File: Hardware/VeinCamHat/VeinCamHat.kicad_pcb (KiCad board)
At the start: 2 copper layers, 65 x 56 mm, 23 parts, among them J1 Raspberry_Pi_2_3, Q1 NTJD4001N

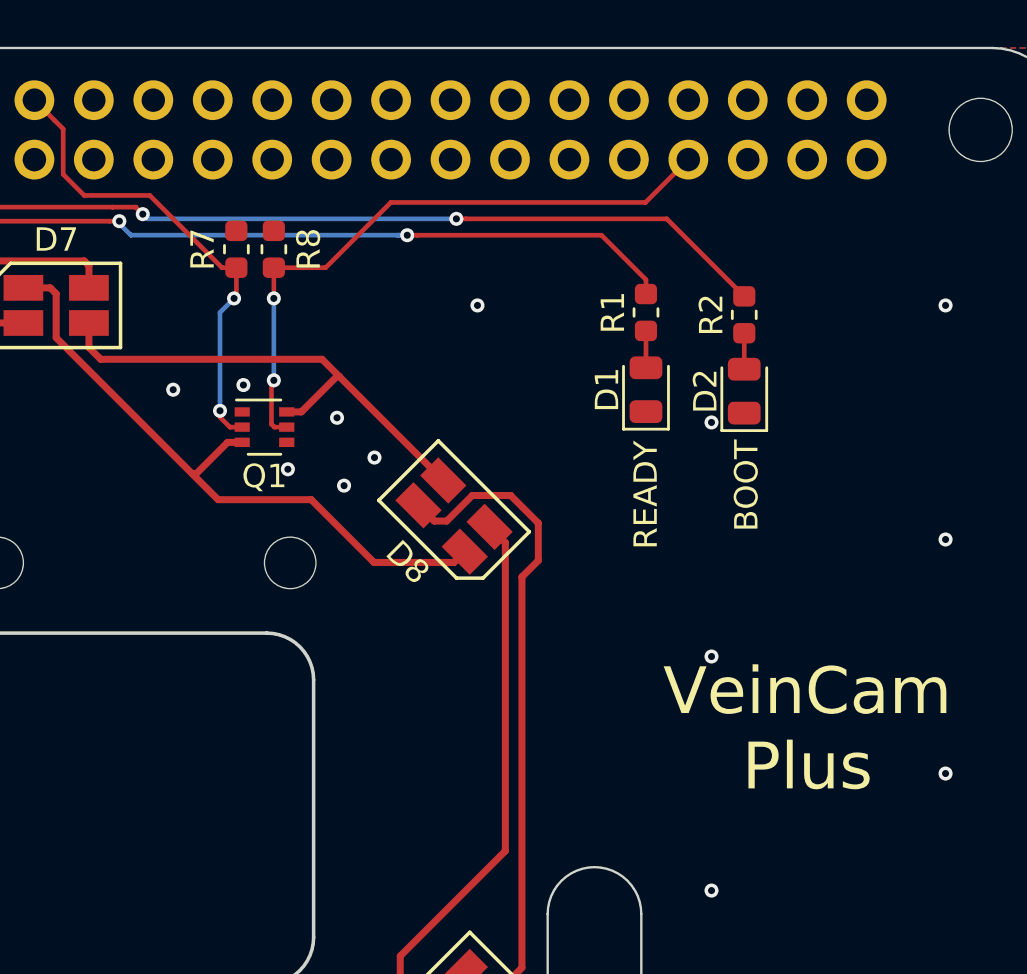
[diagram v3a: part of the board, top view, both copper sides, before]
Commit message: Finished boards, v0.2 gerbers zipped and sent off to fab
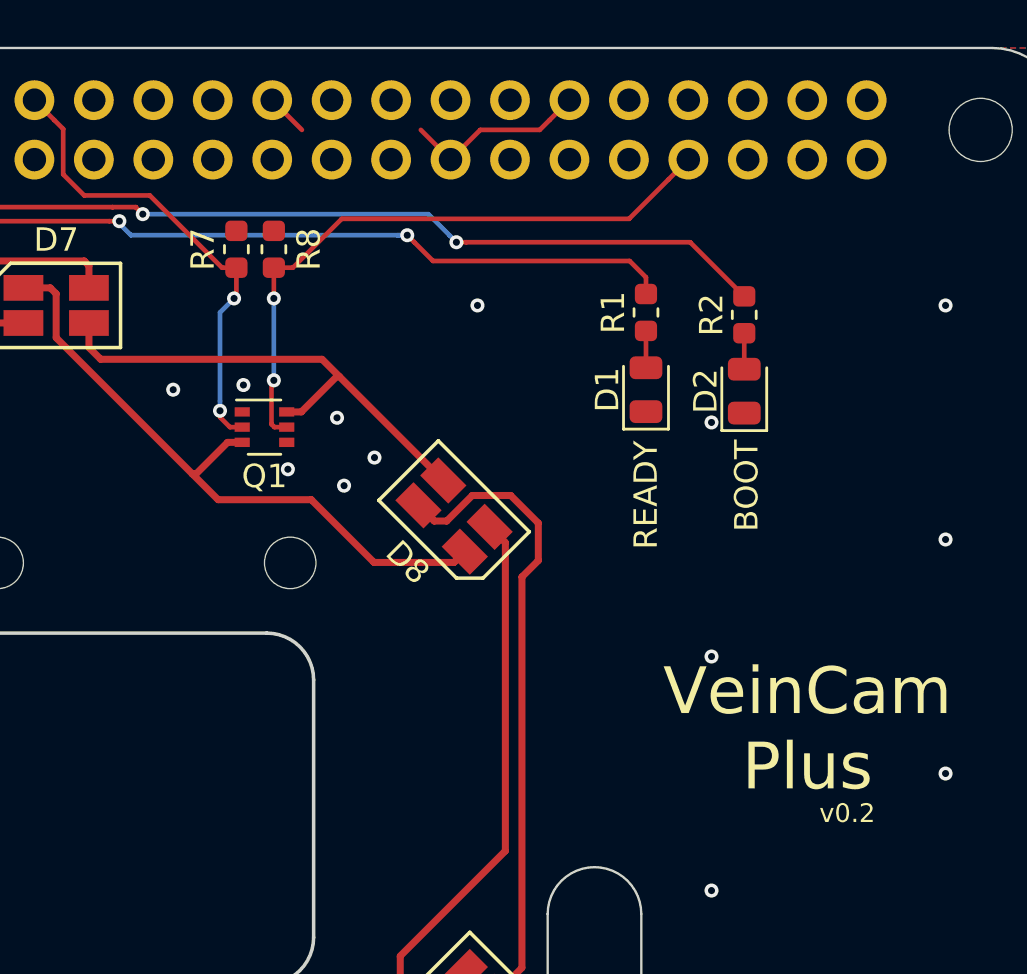
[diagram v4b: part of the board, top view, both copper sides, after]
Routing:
- net GND: track 0.00 -> 9.72 mm
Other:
- board text added: "v0.2"
- board text added: "veincam.org"
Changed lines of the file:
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@@
-(kicad_pcb (version 20171130) (host pcbnew "(5.0.2)-1")
+(kicad_pcb (version 20171130) (host pcbnew "(5.1.0)-1")
   (general
     (thickness 1.6)
-    (drawings 18)
-    (tracks 179)
+    (drawings 20)
+    (tracks 188)
     (zones 0)
     (modules 23)
@@
     (zone_45_only no)
     (trace_min 0.2)
-    (segment_width 0.1)
-    (edge_width 0.1)
     (via_size 0.6)
     (via_drill 0.3)
@@
     (uvia_min_size 0.5)
     (uvia_min_drill 0.1)
+    (edge_width 0.1)
+    (segment_width 0.1)
     (pcb_text_width 0.3)
     (pcb_text_size 1 1)
@@
     (solder_mask_min_width 0.1)
     (aux_axis_origin 200 150)
-    (visible_elements 7FFFF7FF)
+    (visible_elements 7FFFFFFF)
     (pcbplotparams
       (layerselection 0x012f8_ffffffff)
@@
     )
   )
+  (gr_text veincam.org (at 221.9 146.9) (layer B.SilkS)
+    (effects (font (size 1 1) (thickness 0.2)) (justify mirror))
+  )
+  (gr_text v0.2 (at 255.8 126.7) (layer F.SilkS)
+    (effects (font (size 0.8 0.8) (thickness 0.12)))
+  )
   (gr_text "Note: 1.6mm FR4" (at 229.8 154) (layer Cmts.User)
     (effects (font (size 1 1) (thickness 0.25)))
@@
   (via (at 207.4 148.1) (size 0.6) (drill 0.3) (layers F.Cu B.Cu) (net 2))
   (via (at 219.4 148.3) (size 0.6) (drill 0.3) (layers F.Cu B.Cu) (net 2))
+  (segment (start 232.5 97.5) (end 231.23 96.23) (width 0.2) (layer F.Cu) (net 2))
+  (segment (start 238.85 98.77) (end 237.58 97.5) (width 0.2) (layer F.Cu) (net 2))
+  (segment (start 243.080001 97.079999) (end 243.93 96.23) (width 0.2) (layer F.Cu) (net 2))
+  (segment (start 242.66 97.5) (end 243.080001 97.079999) (width 0.2) (layer F.Cu) (net 2))
+  (segment (start 238.85 98.77) (end 240.12 97.5) (width 0.2) (layer F.Cu) (net 2))
+  (segment (start 240.12 97.5) (end 242.66 97.5) (width 0.2) (layer F.Cu) (net 2))
   (segment (start 247.2 106.0875) (end 247.2 107.6625) (width 0.2) (layer F.Cu) (net 3))
   (segment (start 251.4 106.1875) (end 251.4 107.725) (width 0.2) (layer F.Cu) (net 4))
@@
   (segment (start 236.575736 102) (end 237 102) (width 0.2) (layer B.Cu) (net 11))
   (via (at 237 102) (size 0.6) (drill 0.3) (layers F.Cu B.Cu) (net 11))
-  (segment (start 247.2 103.9) (end 245.3 102) (width 0.2) (layer F.Cu) (net 11))
-  (segment (start 247.2 104.5125) (end 247.2 103.9) (width 0.2) (layer F.Cu) (net 11))
-  (segment (start 245.3 102) (end 237.424264 102) (width 0.2) (layer F.Cu) (net 11))
-  (segment (start 237.424264 102) (end 237 102) (width 0.2) (layer F.Cu) (net 11))
   (segment (start 224.275736 101.4) (end 224.7 101.4) (width 0.2) (layer F.Cu) (net 11))
   (segment (start 215.99 98.77) (end 218.62 101.4) (width 0.2) (layer F.Cu) (net 11))
@@
   (segment (start 237 102) (end 225.2 102) (width 0.2) (layer B.Cu) (net 11))
   (via (at 224.7 101.4) (size 0.6) (drill 0.3) (layers F.Cu B.Cu) (net 11))
-  (segment (start 239.524264 101.3) (end 239.1 101.3) (width 0.2) (layer F.Cu) (net 12))
-  (segment (start 248.0875 101.3) (end 239.524264 101.3) (width 0.2) (layer F.Cu) (net 12))
-  (segment (start 251.4 104.6125) (end 248.0875 101.3) (width 0.2) (layer F.Cu) (net 12))
-  (via (at 239.1 101.3) (size 0.6) (drill 0.3) (layers F.Cu B.Cu) (net 12))
+  (segment (start 237.299999 102.299999) (end 237 102) (width 0.2) (layer F.Cu) (net 11))
+  (segment (start 238.1 103.1) (end 237.299999 102.299999) (width 0.2) (layer F.Cu) (net 11))
+  (segment (start 246.5 103.1) (end 238.1 103.1) (width 0.2) (layer F.Cu) (net 11))
+  (segment (start 247.2 104.5125) (end 247.2 103.8) (width 0.2) (layer F.Cu) (net 11))
+  (segment (start 247.2 103.8) (end 246.5 103.1) (width 0.2) (layer F.Cu) (net 11))
   (via (at 225.7 101.1) (size 0.6) (drill 0.3) (layers F.Cu B.Cu) (net 12))
-  (segment (start 225.9 101.3) (end 225.7 101.1) (width 0.2) (layer B.Cu) (net 12))
-  (segment (start 239.1 101.3) (end 225.9 101.3) (width 0.2) (layer B.Cu) (net 12))
   (segment (start 218.857999 100.800001) (end 224.411997 100.800001) (width 0.2) (layer F.Cu) (net 12))
   (segment (start 217.140001 99.082003) (end 218.857999 100.800001) (width 0.2) (layer F.Cu) (net 12))
@@
   (segment (start 215.99 96.23) (end 217.140001 97.380001) (width 0.2) (layer F.Cu) (net 12))
   (segment (start 217.140001 97.380001) (end 217.140001 99.082003) (width 0.2) (layer F.Cu) (net 12))
+  (segment (start 237.899998 101.1) (end 238.800001 102.000003) (width 0.2) (layer B.Cu) (net 12))
+  (segment (start 238.800001 102.000003) (end 239.1 102.300002) (width 0.2) (layer B.Cu) (net 12))
+  (segment (start 251.4 104.6125) (end 249.087502 102.300002) (width 0.2) (layer F.Cu) (net 12))
+  (segment (start 239.524264 102.300002) (end 239.1 102.300002) (width 0.2) (layer F.Cu) (net 12))
+  (segment (start 249.087502 102.300002) (end 239.524264 102.300002) (width 0.2) (layer F.Cu) (net 12))
+  (segment (start 225.7 101.1) (end 237.899998 101.1) (width 0.2) (layer B.Cu) (net 12))
+  (via (at 239.1 102.300002) (size 0.6) (drill 0.3) (layers F.Cu B.Cu) (net 12))
   (via (at 229.6 104.7) (size 0.6) (drill 0.3) (layers F.Cu B.Cu) (net 13))
   (segment (start 229.7 104.6) (end 229.7 103.3875) (width 0.2) (layer F.Cu) (net 13))
@@
   (segment (start 231.85 110.2) (end 231.325 110.2) (width 0.2) (layer F.Cu) (net 14))
   (segment (start 231.325 110.2) (end 231.2 110.075) (width 0.2) (layer F.Cu) (net 14))
-  (segment (start 247.18 100.6) (end 249.01 98.77) (width 0.2) (layer F.Cu) (net 14))
-  (segment (start 236.3 100.6) (end 247.18 100.6) (width 0.2) (layer F.Cu) (net 14))
-  (segment (start 231.3 103.3875) (end 233.5125 103.3875) (width 0.2) (layer F.Cu) (net 14))
-  (segment (start 233.5125 103.3875) (end 236.3 100.6) (width 0.2) (layer F.Cu) (net 14))
+  (segment (start 248.160001 99.619999) (end 249.01 98.77) (width 0.2) (layer F.Cu) (net 14))
+  (segment (start 246.48 101.3) (end 248.160001 99.619999) (width 0.2) (layer F.Cu) (net 14))
+  (segment (start 234.2 101.3) (end 246.48 101.3) (width 0.2) (layer F.Cu) (net 14))
+  (segment (start 231.3 103.3875) (end 232.1125 103.3875) (width 0.2) (layer F.Cu) (net 14))
+  (segment (start 232.1125 103.3875) (end 234.2 101.3) (width 0.2) (layer F.Cu) (net 14))
   (segment (start 202.5 135.520101) (end 203.47972 134.540381) (width 0.3) (layer F.Cu) (net 15))
   (segment (start 210.4125 145.2) (end 202.5 137.2875) (width 0.3) (layer F.Cu) (net 15))

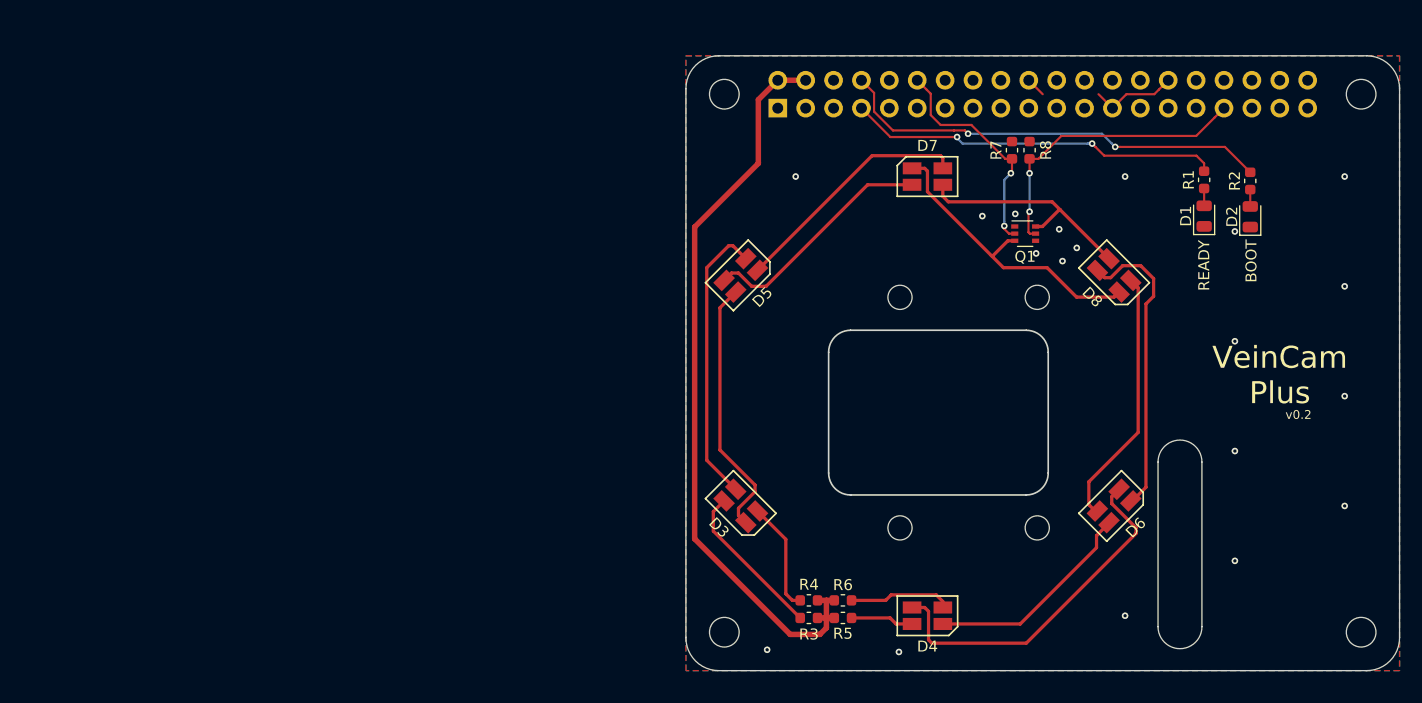
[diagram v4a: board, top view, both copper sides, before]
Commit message: changed logo direction on veincam, added licencing document
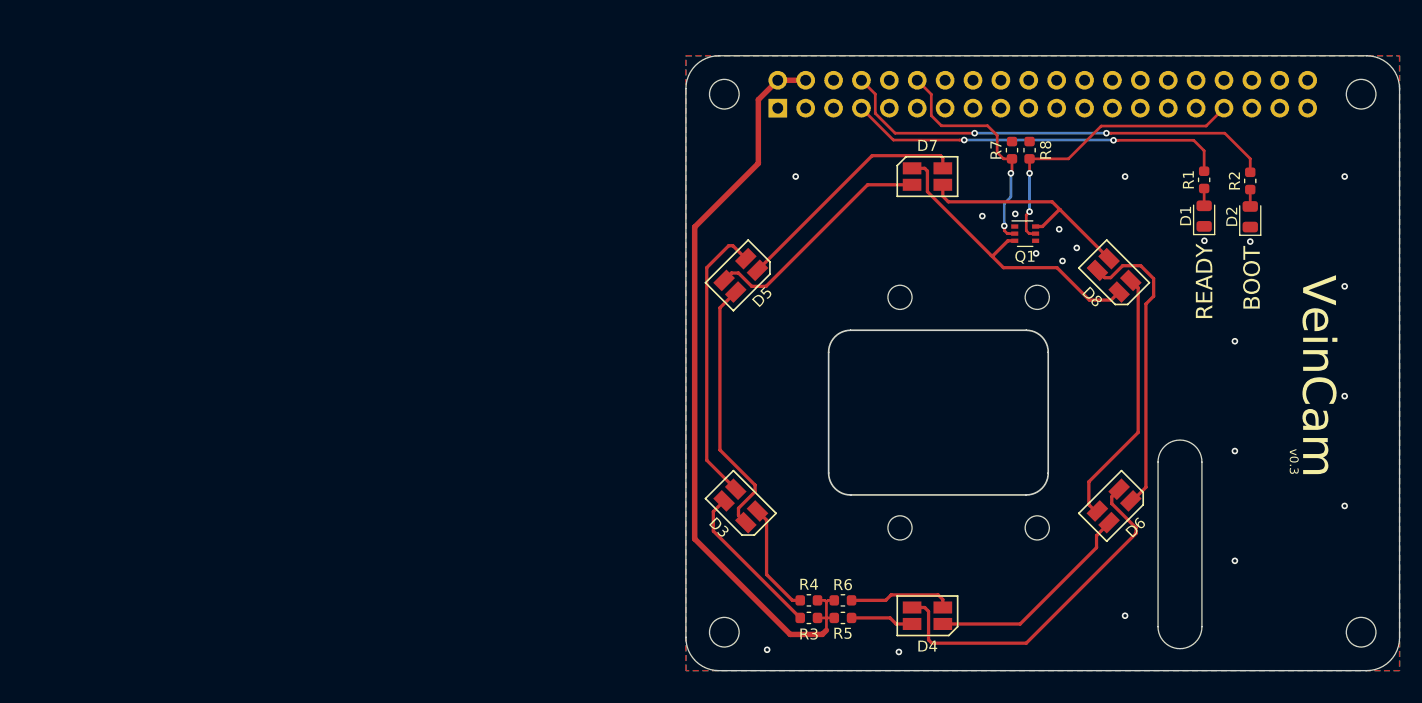
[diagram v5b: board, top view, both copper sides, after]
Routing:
- net GND: track 9.72 -> 0.00 mm, vias 19 -> 20
- net /LED_940: track 20.5 -> 21.5 mm
- net /LED_BOOT: track 39.9 -> 40.6 mm
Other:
- board text added: "VeinCam"
- board text added: "v0.3"
- board text removed: "VeinCam Plus"
- board text removed: "v0.2"

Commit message: More schematic / PCB changes
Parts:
- R2: value 1k -> 1k5
- moved D2 4.51 mm to (246.9, 108.4), turned to 270 degrees
- moved R2 4.51 mm to (246.9, 105.2), turned to 90 degrees
- moved D1 3.36 mm to (250.6, 108.4)
- moved R1 3.34 mm to (250.5, 105.2), turned to 90 degrees
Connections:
- D2 pad 1: GND -> /nLED_BOOT
- D2 pad 2: Net-(D2-Pad2) -> +3V3
- J1 pad 1: Net-(J1-Pad1) -> (no net)
- J1 pad 10: Net-(J1-Pad10) -> (no net)
- J1 pad 11: Net-(J1-Pad11) -> (no net)
- J1 pad 13: Net-(J1-Pad13) -> (no net)
- J1 pad 15: Net-(J1-Pad15) -> (no net)
- J1 pad 16: Net-(J1-Pad16) -> (no net)
- J1 pad 17: Net-(J1-Pad17) -> +3V3
- J1 pad 18: Net-(J1-Pad18) -> (no net)
- J1 pad 19: Net-(J1-Pad19) -> (no net)
- J1 pad 21: Net-(J1-Pad21) -> (no net)
- J1 pad 22: Net-(J1-Pad22) -> (no net)
- J1 pad 23: Net-(J1-Pad23) -> (no net)
- J1 pad 24: Net-(J1-Pad24) -> (no net)
- J1 pad 26: Net-(J1-Pad26) -> (no net)
- J1 pad 27: Net-(J1-Pad27) -> (no net)
- J1 pad 28: Net-(J1-Pad28) -> (no net)
- J1 pad 29: Net-(J1-Pad29) -> (no net)
- J1 pad 3: Net-(J1-Pad3) -> (no net)
- J1 pad 31: Net-(J1-Pad31) -> (no net)
- J1 pad 32: Net-(J1-Pad32) -> (no net)
- J1 pad 35: Net-(J1-Pad35) -> /nLED_BOOT
- J1 pad 36: Net-(J1-Pad36) -> (no net)
- J1 pad 37: Net-(J1-Pad37) -> /LED_READY
- J1 pad 38: Net-(J1-Pad38) -> (no net)
- J1 pad 40: Net-(J1-Pad40) -> (no net)
- J1 pad 5: Net-(J1-Pad5) -> (no net)
- J1 pad 7: /LED_READY -> (no net)
- J1 pad 8: /LED_BOOT -> (no net)
- R1 pad 1: /LED_READY -> Net-(D1-Pad2)
- R1 pad 2: Net-(D1-Pad2) -> /LED_READY
- R2 pad 1: /LED_BOOT -> /nLED_BOOT
- R2 pad 2: Net-(D2-Pad2) -> GND
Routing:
- net /LED_BOOT: track 40.6 -> 0.00 mm, vias 2 -> 0
- net /LED_READY: track 34.7 -> 7.14 mm, vias 2 -> 0
- net +3V3: track 0.00 -> 25.7 mm, vias 0 -> 1
- net /nLED_BOOT: track 0.00 -> 10.9 mm
- net GND: track 0.00 -> 3.65 mm, vias 20 -> 23
- net Net-(D4-Pad3): track 32.6 -> 30.2 mm
- net Net-(D2-Pad2): track 1.54 -> 0.00 mm
- net Net-(D6-Pad1): track 27.7 -> 26.8 mm
- net Net-(D3-Pad3): track 26.2 -> 25.3 mm
- net Net-(D4-Pad1): track 20.0 -> 19.3 mm
- net /LED_940: track 21.5 -> 21.0 mm
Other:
- board text removed: "Note: 1.6mm FR4"

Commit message: updating hardware things
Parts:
- R1: value 1k -> 1K
- R2: value 1k5 -> 1K5
- R7, R8: value 10k -> 10K
- turned R2 to 270 degrees
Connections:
- D2 pad 1: /nLED_BOOT -> Net-(D2-Pad1)
- J1 pad 12: /LED_940 -> /LED_850
- J1 pad 33: /LED_850 -> /LED_940
- Q1 pad 2: /LED_940 -> /LED_850
- Q1 pad 5: /LED_850 -> /LED_940
- R2 pad 2: GND -> Net-(D2-Pad1)
- R7 pad 1: /LED_940 -> /LED_850
- R8 pad 1: /LED_850 -> /LED_940
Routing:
- net /LED_940: track 21.0 -> 27.7 mm
- net /LED_850: track 27.7 -> 21.0 mm
- net /nLED_BOOT: track 10.9 -> 7.57 mm
- net Net-(D2-Pad1): track 0.00 -> 1.56 mm
- net GND: track 3.65 -> 2.84 mm, vias 23 -> 22

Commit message: Updates to board and generation of final production outputs
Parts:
- removed R3, R4, R5, R6: 3R3, Resistor_SMD:R_0603_1608Metric
- added RN1: R_Pack_3R3, Resistor_SMD:R_Array_Convex_4x0603, F.Cu at (212.2, 145.1)
- moved D5 3.30 mm to (205.1, 117.3)
- moved D8 3.30 mm to (238.9, 117.3)
- moved D7 2.00 mm to (222.0, 107.0)
- moved D2 1.50 mm to (248.4, 108.5)
- moved D1 1.50 mm to (252.1, 108.5)
- moved R1 1.50 mm to (252.0, 105.3)
- moved R2 1.50 mm to (248.4, 105.2)
- moved Q1 1.00 mm to (231.9, 110.2)
- moved D3 0.32 mm to (205.1, 134.7)
- moved D6 0.32 mm to (238.9, 134.7)
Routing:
- net Net-(D3-Pad1): track 23.8 -> 19.6 mm
- net Net-(D3-Pad3): track 25.3 -> 21.3 mm
- net Net-(D6-Pad3): track 23.9 -> 19.9 mm
- net Net-(D4-Pad4): track 9.42 -> 13.0 mm
- net Net-(D4-Pad2): track 5.74 -> 9.12 mm
- net Net-(D6-Pad1): track 26.8 -> 23.5 mm
- net +3V3: track 26.2 -> 27.8 mm
- net Net-(D3-Pad4): track 10.2 -> 11.2 mm
- net Net-(D7-Pad1): track 27.9 -> 27.0 mm
- net Net-(D3-Pad2): track 14.3 -> 13.5 mm
- net /LED_940: track 27.7 -> 28.4 mm
- net /LED_READY: track 7.14 -> 6.57 mm
- net /nLED_BOOT: track 7.57 -> 7.03 mm
- net GND: vias 22 -> 18
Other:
- board text removed: "v0.3"
- board text removed: "veincam.org"
